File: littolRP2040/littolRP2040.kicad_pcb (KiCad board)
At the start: 2 copper layers, 209.6 x 66.7 mm, 81 parts, among them J1 USB_C_Receptacle_USB2.0, J2 Conn_01x05, U1 SRV05-4, U2 XC6206PxxxMR, U3 W25Q128JVS, U4 RP2040, Y1 X322512MSB4SI

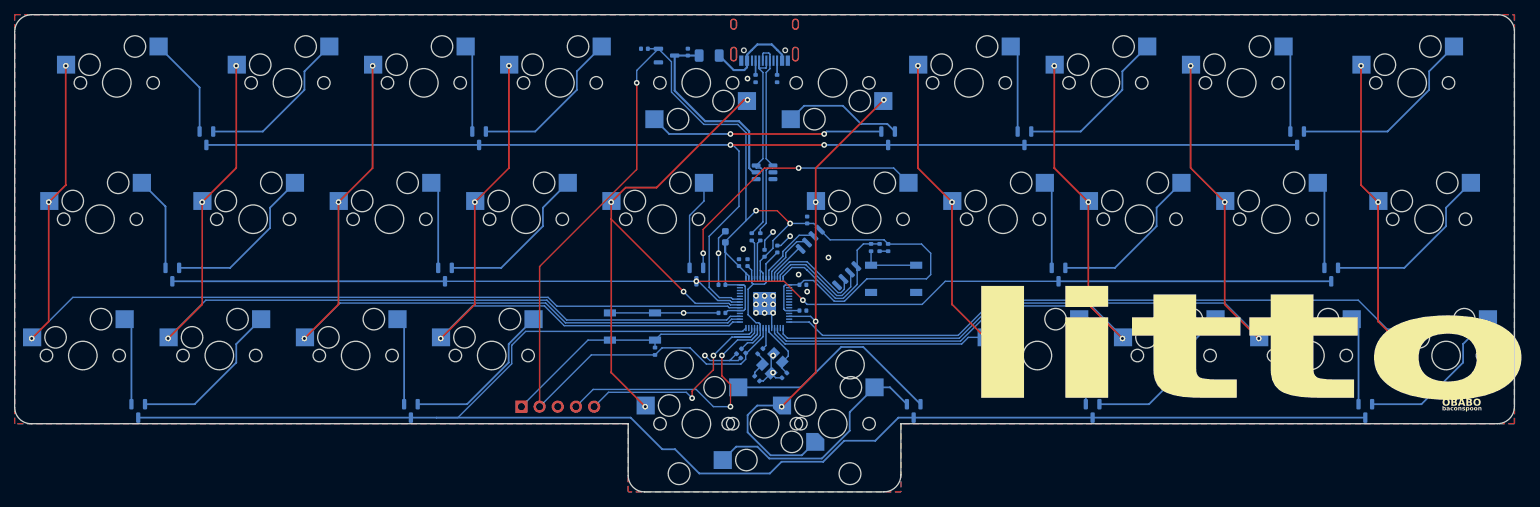
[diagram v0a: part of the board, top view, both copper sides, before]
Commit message: PCB cleanup. Updated fabrication files. Added BOM and position files for JLCPCB fabrication.
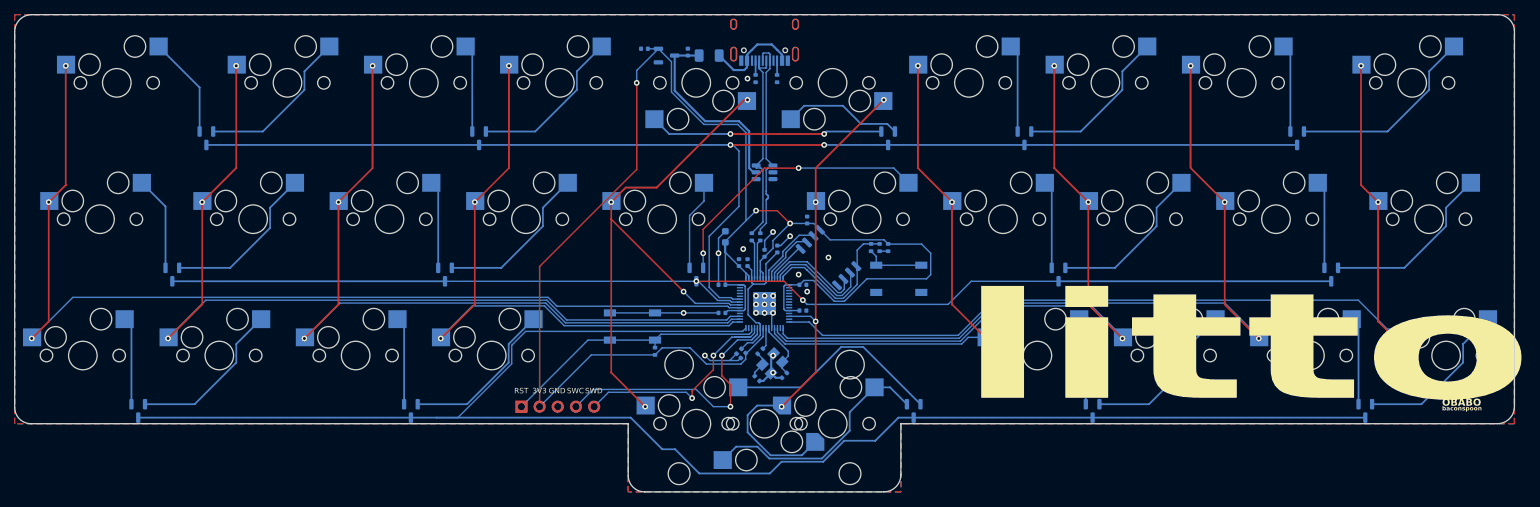
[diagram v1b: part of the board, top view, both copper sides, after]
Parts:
- F1: value Fuse_Small -> 500mA
- J1: value USB_C_Receptacle_USB2.0 -> TYPE-C-31-M-12
- MX1, MX10, MX11, MX12, MX13, MX14, MX15, MX16, MX17, MX18, MX19, MX2, MX20, MX21, MX22, MX23, MX24, MX25, MX26, MX27, MX28, MX29, MX3, MX30, MX31, MX4, MX5, MX6, MX7, MX8, MX9: value MX-NoLED -> CPG151101S11; moved to B.Cu
- RESET1: value Reset -> RESET
- U2: value XC6206PxxxMR -> XC6206P332MR
- U3: value W25Q128JVS -> W25Q128JVSIM
- moved BOOT1 0.72 mm to (171.2, 102.4)
- turned MX1 to 180 degrees
- turned MX10 to 180 degrees
- turned MX11 to 180 degrees
- turned MX12 to 180 degrees
- turned MX13 to 0 degrees
- turned MX14 to 180 degrees
- turned MX15 to 180 degrees
- turned MX16 to 0 degrees
- turned MX17 to 180 degrees
- turned MX18 to 180 degrees
- turned MX19 to 0 degrees
- turned MX2 to 180 degrees
- turned MX20 to 180 degrees
- turned MX21 to 180 degrees
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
